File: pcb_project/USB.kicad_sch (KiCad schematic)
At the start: 7 parts, among them J7 USB_A, U3 TPS2041B, U4 D3V3XA4B10LP

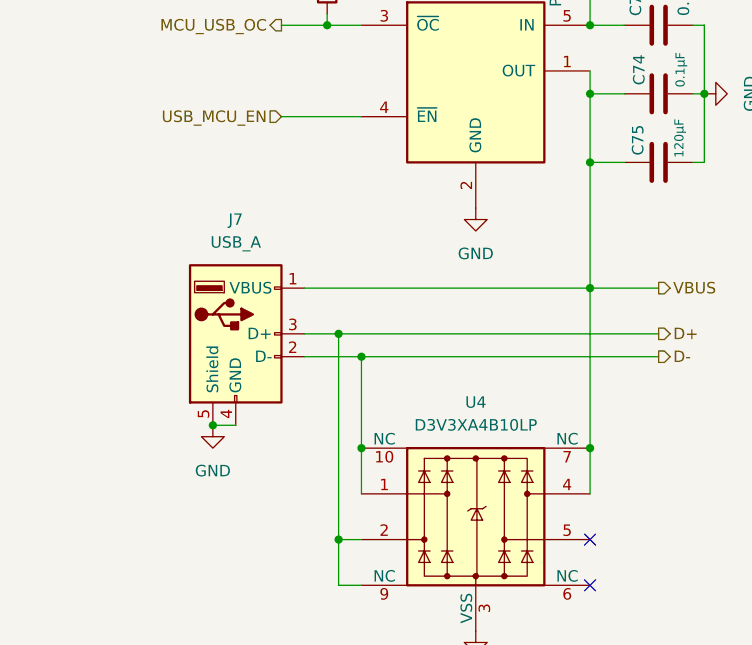
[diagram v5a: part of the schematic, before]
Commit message: Layout with proper USB component
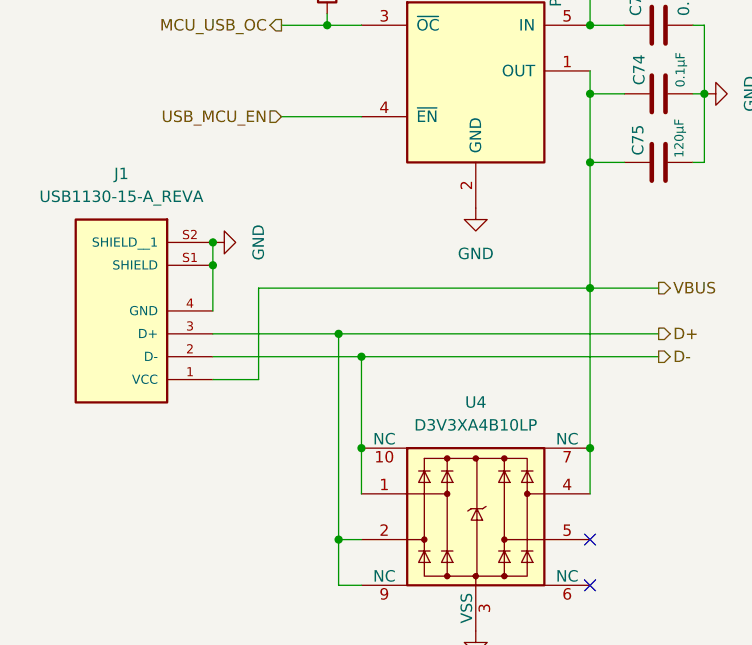
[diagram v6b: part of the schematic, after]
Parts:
- removed J7: USB_A, Connector_USB:USB_A_Wuerth_614004134726_Horizontal, symbol Connector:USB_A
- added J1: USB1130-15-A_REVA, Project_Footprints:GCT_USB1130-15-A_REVA, symbol USB1130-15-A_REVA:USB1130-15-A_REVA
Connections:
- net D+: now also J1.3 (D+)
- net D-: now also J1.2 (D-)
- net GND: now also J1.4 (GND), J1.S1 (SHIELD), J1.S2 (SHIELD__1)
- net VBUS: now also J1.1 (VCC)
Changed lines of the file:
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@@
+	)
+	(junction
+		(at 97.79 96.52)
+		(diameter 0)
+		(color 0 0 0 0)
 	)
 	(junction
@@
 	)
 	(junction
+		(at 97.79 93.98)
+		(diameter 0)
+		(color 0 0 0 0)
+	)
+	(junction
 		(at 139.7 99.06)
 		(diameter 0)
@@
 	(junction
 		(at 114.3 106.68)
-		(diameter 0)
-		(color 0 0 0 0)
-	)
-	(junction
-		(at 97.79 114.3)
 		(diameter 0)
 		(color 0 0 0 0)
@@
 	(wire
 		(pts
+			(xy 97.79 109.22) (xy 102.87 109.22)
+		)
+		(stroke
+			(width 0)
+			(type default)
+		)
+	)
+	(wire
+		(pts
 			(xy 111.76 127) (xy 114.3 127)
 		)
@@
 	(wire
 		(pts
+			(xy 97.79 93.98) (xy 97.79 96.52)
+		)
+		(stroke
+			(width 0)
+			(type default)
+		)
+	)
+	(wire
+		(pts
 			(xy 111.76 132.08) (xy 114.3 132.08)
 		)
@@
 	(wire
 		(pts
-			(xy 107.95 99.06) (xy 139.7 99.06)
-		)
-		(stroke
-			(width 0)
-			(type default)
-		)
-	)
-	(wire
-		(pts
 			(xy 139.7 121.92) (xy 139.7 116.84)
 		)
@@
 	(wire
 		(pts
-			(xy 107.95 104.14) (xy 111.76 104.14)
+			(xy 97.79 96.52) (xy 97.79 101.6)
 		)
 		(stroke
@@
 	(wire
 		(pts
-			(xy 100.33 114.3) (xy 97.79 114.3)
-		)
-		(stroke
-			(width 0)
-			(type default)
-		)
-	)
-	(wire
-		(pts
 			(xy 139.7 85.09) (xy 139.7 99.06)
 		)
@@
 	(wire
 		(pts
-			(xy 107.95 106.68) (xy 114.3 106.68)
-		)
-		(stroke
-			(width 0)
-			(type default)
-		)
-	)
-	(wire
-		(pts
 			(xy 111.76 104.14) (xy 147.32 104.14)
 		)
@@
 	(wire
 		(pts
+			(xy 97.79 106.68) (xy 114.3 106.68)
+		)
+		(stroke
+			(width 0)
+			(type default)
+		)
+	)
+	(wire
+		(pts
 			(xy 152.4 85.09) (xy 151.13 85.09)
 		)
@@
 	(wire
 		(pts
+			(xy 97.79 104.14) (xy 111.76 104.14)
+		)
+		(stroke
+			(width 0)
+			(type default)
+		)
+	)
+	(wire
+		(pts
 			(xy 152.4 69.85) (xy 152.4 77.47)
 		)
@@
 	(wire
 		(pts
+			(xy 102.87 109.22) (xy 102.87 99.06)
+		)
+		(stroke
+			(width 0)
+			(type default)
+		)
+	)
+	(wire
+		(pts
 			(xy 139.7 116.84) (xy 139.7 99.06)
+		)
+		(stroke
+			(width 0)
+			(type default)
+		)
+	)
+	(wire
+		(pts
+			(xy 102.87 99.06) (xy 139.7 99.06)
 		)
 		(stroke
@@
 			)
 			(justify right)
+		)
+	)
+	(symbol
+		(lib_id "USB1130-15-A_REVA:USB1130-15-A_REVA")
+		(at 87.63 104.14 180)
+		(unit 1)
+		(exclude_from_sim no)
+		(in_bom yes)
+		(on_board yes)
+		(dnp no)
+		(fields_autoplaced yes)
+		(property "Reference" "J1"
+			(at 87.63 86.36 0)
+			(effects
+				(font
+					(size 1.27 1.27)
+				)
+			)
+		)
+		(property "Value" "USB1130-15-A_REVA"
+			(at 87.63 88.9 0)
+			(effects
+				(font
+					(size 1.27 1.27)
+				)
+			)
+		)
+		(property "Footprint" "Project_Footprints:GCT_USB1130-15-A_REVA"
+			(at 87.63 104.14 0)
+			(effects
+				(font
+					(size 1.27 1.27)
+				)
+				(justify bottom)
+				(hide yes)
+			)
+		)
+		(property "Datasheet" ""
+			(at 87.63 104.14 0)
+			(effects
+				(font
+					(size 1.27 1.27)
+				)
+				(hide yes)
+			)
+		)
+		(property "Description" ""
+			(at 87.63 104.14 0)
+			(effects
+				(font
+					(size 1.27 1.27)
+				)
+				(hide yes)
+			)
+		)
+		(property "PARTREV" "A"
+			(at 87.63 104.14 0)
+			(effects
+				(font
+					(size 1.27 1.27)
+				)
+				(justify bottom)
+				(hide yes)
+			)
+		)
+		(property "MANUFACTURER" "GCT"
+			(at 87.63 104.14 0)
+			(effects
+				(font
+					(size 1.27 1.27)
+				)
+				(justify bottom)
+				(hide yes)
+			)
+		)
+		(property "MAXIMUM_PACKAGE_HEIGHT" "7.24mm"
+			(at 87.63 104.14 0)
+			(effects
+				(font
+					(size 1.27 1.27)
+				)
+				(justify bottom)
+				(hide yes)
+			)
+		)
+		(property "STANDARD" "Manufacturer Recommendations"
+			(at 87.63 104.14 0)
+			(effects
+				(font
+					(size 1.27 1.27)
+				)
+				(justify bottom)
+				(hide yes)
+			)
+		)
+		(pin "S1"
+		)
+		(pin "S2"
+		)
+		(pin "2"
+		)
+		(pin "3"
+		)
+		(pin "4"
+		)
+		(pin "1"
+		)
+		(instances
+			(project ""
+				(path "/98f80f66-4595-4d0f-90ca-59b2db6f447b/d8354ada-74b3-4c6a-8679-c8f4ff1d8cd0"
+					(reference "J1")
+					(unit 1)
+				)
+			)
 		)
 	)
@@
 	)
 	(symbol
-		(lib_id "Connector:USB_A")
-		(at 100.33 104.14 0)
-		(unit 1)
-		(exclude_from_sim no)
-		(in_bom yes)
-		(on_board yes)
-		(dnp no)
-		(fields_autoplaced yes)
-		(property "Reference" "J7"
-			(at 100.33 91.44 0)
-			(effects
-				(font
-					(size 1.27 1.27)
-				)
-			)
-		)
-		(property "Value" "USB_A"
-			(at 100.33 93.98 0)
-			(effects
-				(font
-					(size 1.27 1.27)
-				)
-			)
-		)
-		(property "Footprint" "Connector_USB:USB_A_Wuerth_614004134726_Horizontal"
-			(at 104.14 105.41 0)
-			(effects
-				(font
-					(size 1.27 1.27)
-				)
-				(hide yes)
-			)
-		)
-		(property "Datasheet" "~"
-			(at 104.14 105.41 0)
-			(effects
-				(font
-					(size 1.27 1.27)
-				)
-				(hide yes)
-			)
-		)
-		(property "Description" "USB Type A connector"
-			(at 100.33 104.14 0)
-			(effects
-				(font
-					(size 1.27 1.27)
-				)
-				(hide yes)
-			)
-		)
-		(pin "4"
-		)
-		(pin "1"
-		)
-		(pin "3"
-		)
-		(pin "2"
-		)
-		(pin "5"
-		)
-		(instances
-			(project "pcb_project"
-				(path "/98f80f66-4595-4d0f-90ca-59b2db6f447b/d8354ada-74b3-4c6a-8679-c8f4ff1d8cd0"
-					(reference "J7")
-					(unit 1)
-				)
-			)
-		)
-	)
-	(symbol
 		(lib_id "Device:C")
 		(at 147.32 85.09 270)
@@
 	(symbol
 		(lib_id "power:GND")
-		(at 97.79 114.3 0)
+		(at 97.79 93.98 90)
 		(unit 1)
 		(exclude_from_sim no)
@@
 		(fields_autoplaced yes)
 		(property "Reference" "#PWR079"
-			(at 97.79 120.65 0)
+			(at 104.14 93.98 0)
 			(effects
 				(font
@@
 		)
 		(property "Value" "GND"
-			(at 97.79 119.38 0)
+			(at 102.87 93.98 0)
 			(effects
 				(font
@@
 		)
 		(property "Footprint" ""
-			(at 97.79 114.3 0)
+			(at 97.79 93.98 0)
 			(effects
 				(font
@@
 		)
 		(property "Datasheet" ""
-			(at 97.79 114.3 0)
+			(at 97.79 93.98 0)
 			(effects
 				(font
@@
 		)
 		(property "Description" "Power symbol creates a global label with name \"GND\" , ground"
-			(at 97.79 114.3 0)
-			(effects
-				(font
+			(at 97.79 93.98 0)
+			(effects
+				(font
